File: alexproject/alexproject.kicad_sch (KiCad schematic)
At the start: 18 parts, among them J1 Conn_01x03_Pin, Q1 NMOS, Q2 NMOS

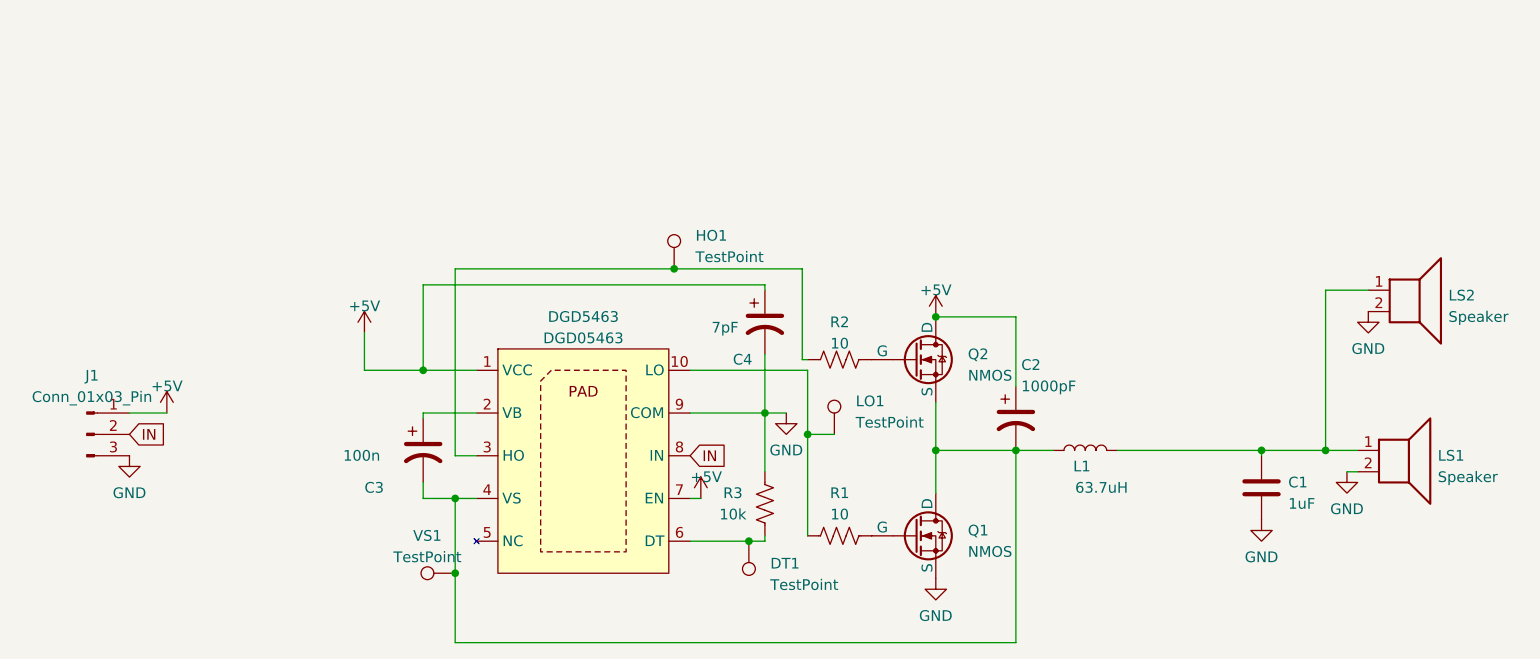
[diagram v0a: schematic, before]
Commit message: testing spice sim & updated PCB
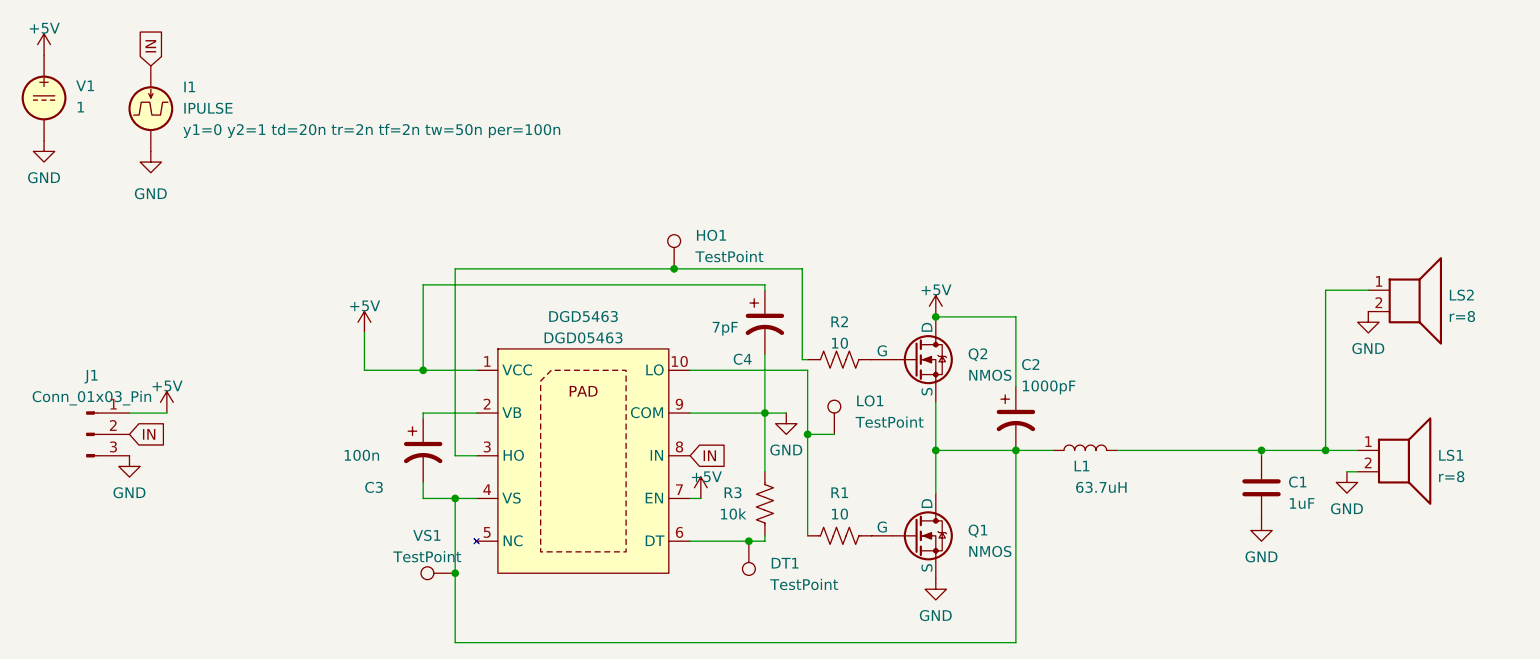
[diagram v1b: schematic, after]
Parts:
- added I1: IPULSE, symbol Simulation_SPICE:IPULSE
- added V1: 1, symbol Simulation_SPICE:VDC
- LS1, LS2: value Speaker -> ${SIM.PARAMS}
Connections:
- net +5V: now also V1.1
- net GND: now also I1.2, V1.2
- net IN: now also I1.1
